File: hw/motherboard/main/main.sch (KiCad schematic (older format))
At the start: 27 parts, among them J1 SWD holes, J2 Conn_ARM_JTAG_SWD_10, J4 STACK_GND, SW1 SW_Push, U1 STM32F303RETx, Y1 HSE

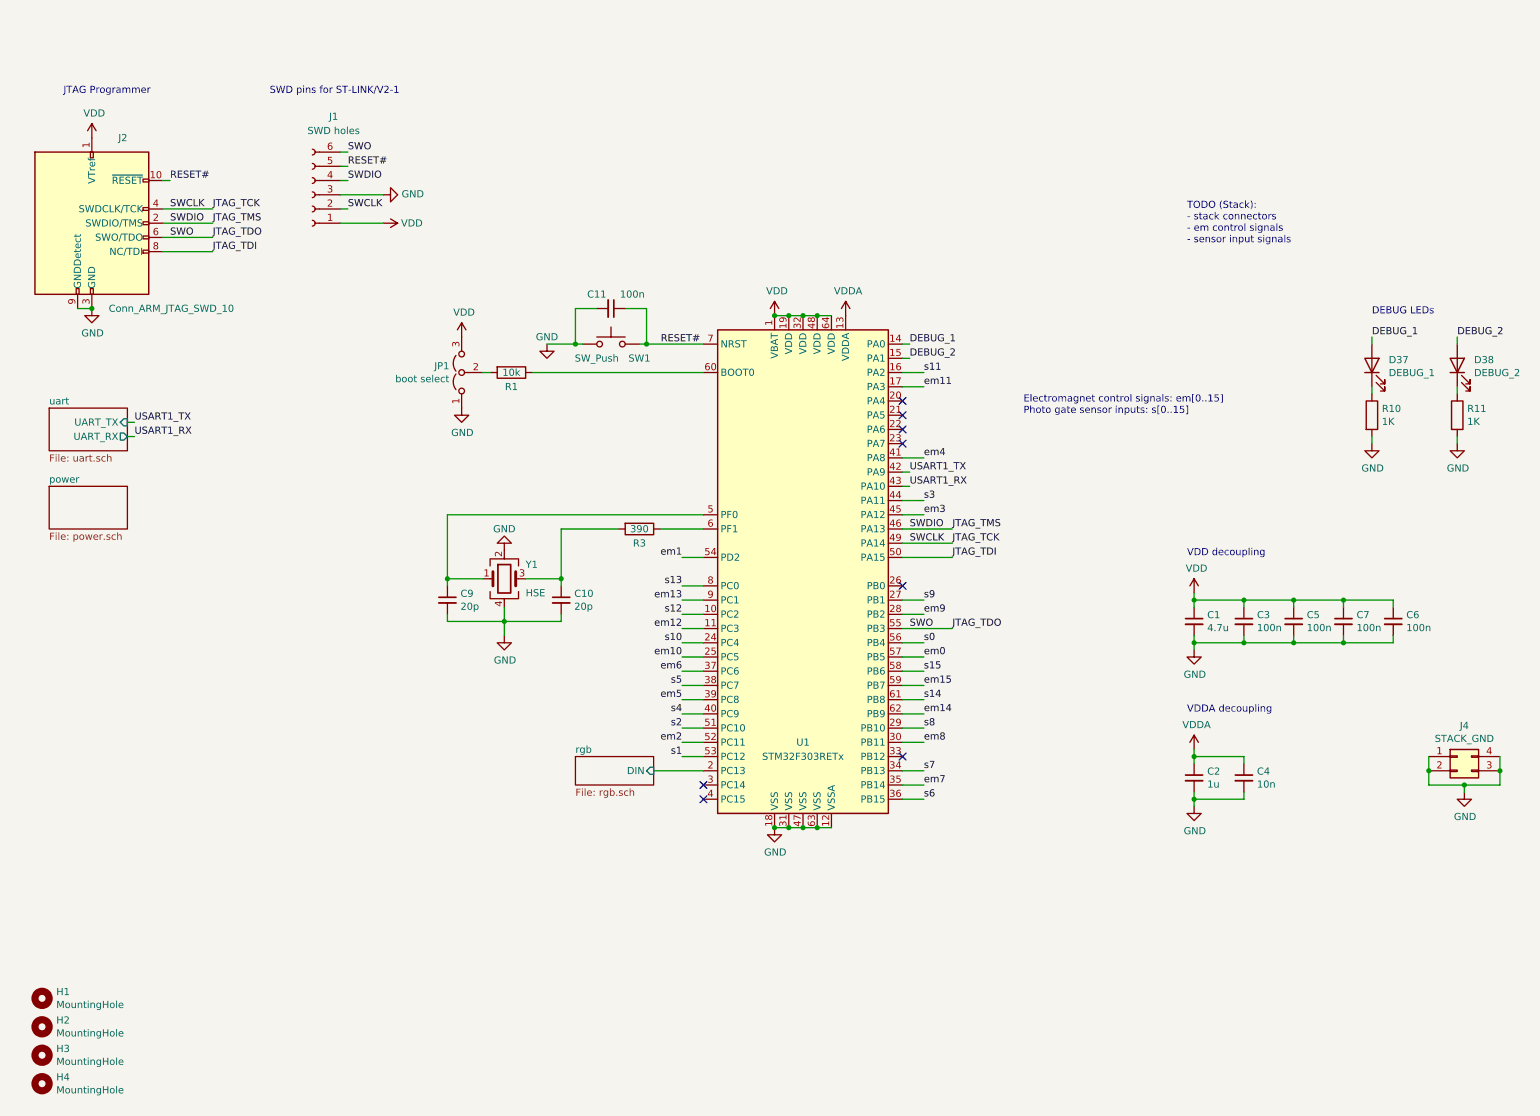
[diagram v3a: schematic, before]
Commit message: Lay out motherboard hardware revision 1
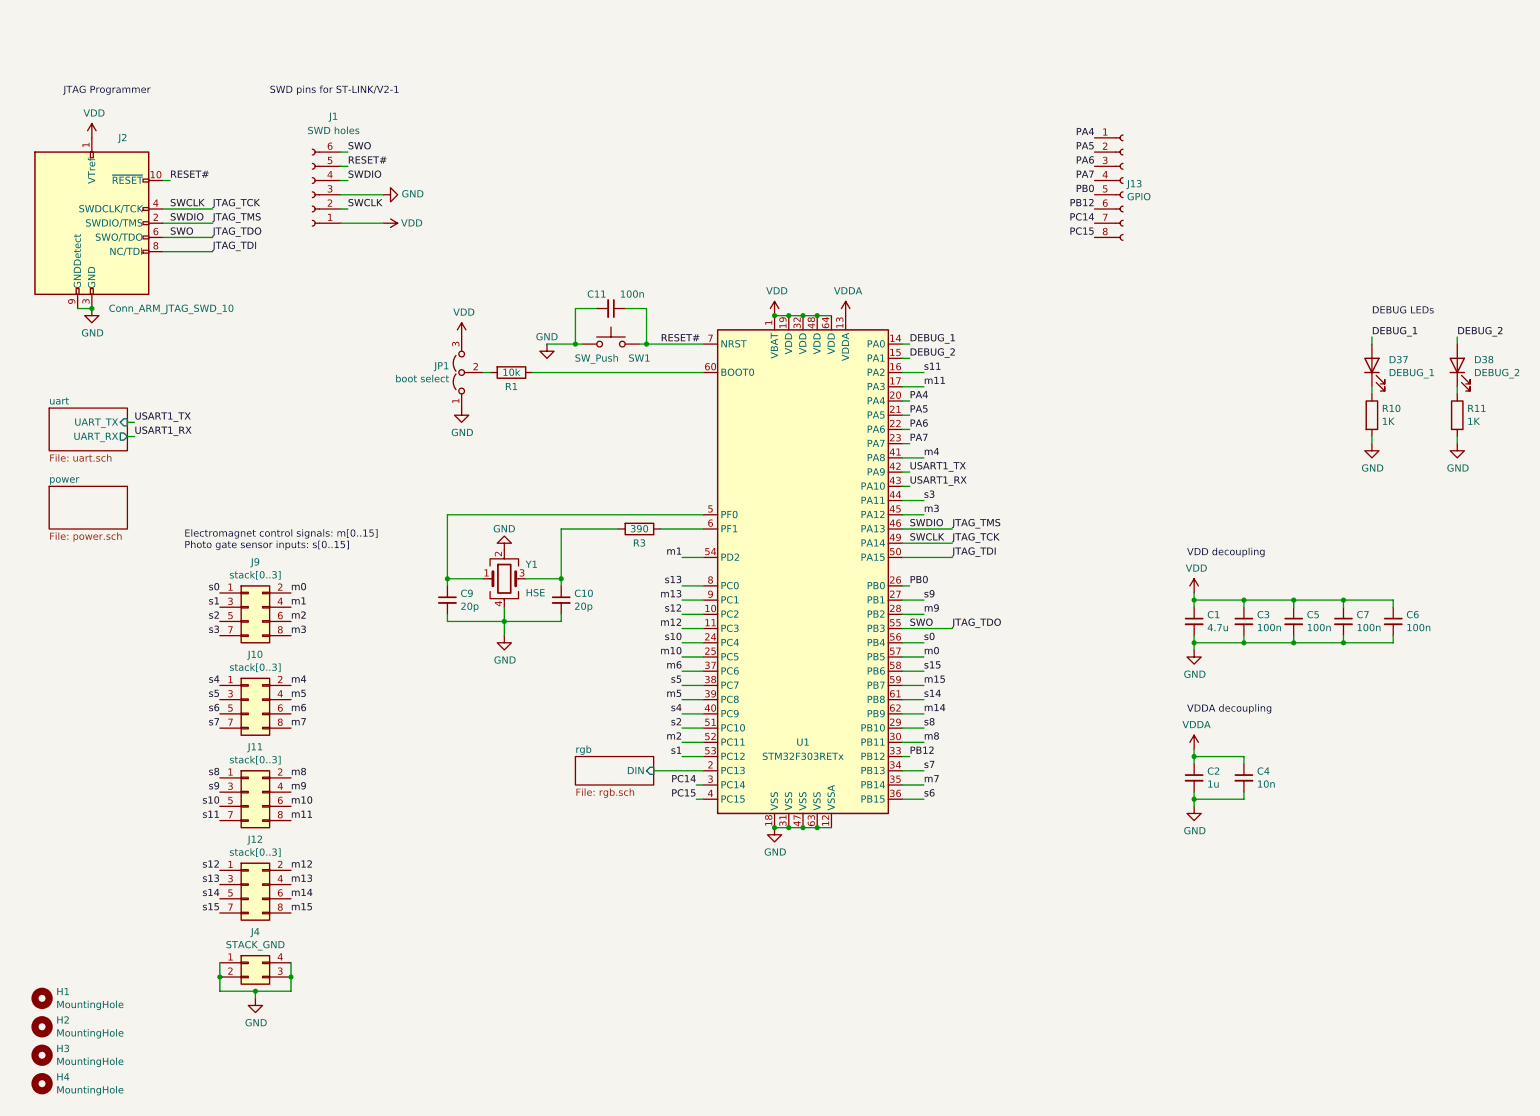
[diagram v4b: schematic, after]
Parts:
- added J10, J11, J12, J9: stack[0..3], Connector_PinSocket_2.54mm:PinSocket_2x04_P2.54mm_Vertical, symbol Connector_Generic:Conn_02x04_Odd_Even
- added J13: GPIO, Connector_PinSocket_2.54mm:PinSocket_1x08_P2.54mm_Vertical, symbol Connector:Conn_01x08_Female
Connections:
- net s0: now also J9.1 (Pin_1)
- net s1: now also J9.3 (Pin_3)
- net s10: now also J11.5 (Pin_5)
- net s11: now also J11.7 (Pin_7)
- net s12: now also J12.1 (Pin_1)
- net s13: now also J12.3 (Pin_3)
- net s14: now also J12.5 (Pin_5)
- net s15: now also J12.7 (Pin_7)
- net s2: now also J9.5 (Pin_5)
- net s3: now also J9.7 (Pin_7)
- net s4: now also J10.1 (Pin_1)
- net s5: now also J10.3 (Pin_3)
- net s6: now also J10.5 (Pin_5)
- net s7: now also J10.7 (Pin_7)
- net s8: now also J11.1 (Pin_1)
- net s9: now also J11.3 (Pin_3)
- net PA4: now reaches U1.20 (PA4)
- net PA4: now also J13.1 (Pin_1)
- net PA5: now reaches U1.21 (PA5)
- net PA5: now also J13.2 (Pin_2)
- net PA6: now reaches U1.22 (PA6)
- net PA6: now also J13.3 (Pin_3)
- net PA7: now reaches U1.23 (PA7)
- net PA7: now also J13.4 (Pin_4)
- net PB0: now reaches U1.26 (PB0)
- net PB0: now also J13.5 (Pin_5)
- net PC14: now reaches U1.3 (PC14)
- net PC14: now also J13.7 (Pin_7)
- net PB12: now reaches U1.33 (PB12)
- net PB12: now also J13.6 (Pin_6)
- net PC15: now reaches U1.4 (PC15)
- net PC15: now also J13.8 (Pin_8)
- net em0 renamed m0
- net m0: now also J9.2 (Pin_2)
- net em1 renamed m1
- net m1: now also J9.4 (Pin_4)
- net em10 renamed m10
- net m10: now also J11.6 (Pin_6)
- net em11 renamed m11
- net m11: now also J11.8 (Pin_8)
- net em12 renamed m12
- net m12: now also J12.2 (Pin_2)
- net em13 renamed m13
- net m13: now also J12.4 (Pin_4)
- net em14 renamed m14
- net m14: now also J12.6 (Pin_6)
- net em15 renamed m15
- net m15: now also J12.8 (Pin_8)
- net em2 renamed m2
- net m2: now also J9.6 (Pin_6)
- net em3 renamed m3
- net m3: now also J9.8 (Pin_8)
- net em4 renamed m4
- net m4: now also J10.2 (Pin_2)
- net em5 renamed m5
- net m5: now also J10.4 (Pin_4)
- net em6 renamed m6
- net m6: now also J10.6 (Pin_6)
- net em7 renamed m7
- net m7: now also J10.8 (Pin_8)
- net em8 renamed m8
- net m8: now also J11.2 (Pin_2)
- net em9 renamed m9
- net m9: now also J11.4 (Pin_4)
- no-connect marks 8 -> 0
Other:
- note added: "Electromagnet control signals: m[0..15]\nPhoto gate sensor inputs: s[0..15]"
- note removed: "Electromagnet control signals: em[0..15]\nPhoto gate sensor inputs: s[0..15]"
- note removed: "TODO (Stack):\n- stack connectors\n- em control signals\n- sensor input signals"
- moved on the sheet: J4

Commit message: Add missing component values.
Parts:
- C1: footprint Capacitor_SMD:C_0603_1608Metric -> Capacitor_SMD:C_0805_2012Metric
- C10, C9: value 20p -> 27p
- R10, R11: value 1K -> 1k
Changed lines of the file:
@@
 F 0 "C1" H 8892 4396 50  0000 L CNN
 F 1 "4.7u" H 8892 4305 50  0000 L CNN
-F 2 "Capacitor_SMD:C_0603_1608Metric" H 8800 4350 50  0001 C CNN
+F 2 "Capacitor_SMD:C_0805_2012Metric" H 8800 4350 50  0001 C CNN
 F 3 "~" H 8800 4350 50  0001 C CNN
 	1    8800 4350
@@
 P 3550 4200
 F 0 "C9" H 3642 4246 50  0000 L CNN
-F 1 "20p" H 3642 4155 50  0000 L CNN
+F 1 "27p" H 3642 4155 50  0000 L CNN
 F 2 "Capacitor_SMD:C_0603_1608Metric" H 3550 4200 50  0001 C CNN
 F 3 "~" H 3550 4200 50  0001 C CNN
@@
 P 4350 4200
 F 0 "C10" H 4442 4246 50  0000 L CNN
-F 1 "20p" H 4442 4155 50  0000 L CNN
+F 1 "27p" H 4442 4155 50  0000 L CNN
 F 2 "Capacitor_SMD:C_0603_1608Metric" H 4350 4200 50  0001 C CNN
 F 3 "~" H 4350 4200 50  0001 C CNN
@@
 P 10650 2900
 F 0 "R11" H 10720 2946 50  0000 L CNN
-F 1 "1K" H 10720 2855 50  0000 L CNN
+F 1 "1k" H 10720 2855 50  0000 L CNN
 F 2 "Resistor_SMD:R_0805_2012Metric" V 10580 2900 50  0001 C CNN
 F 3 "~" H 10650 2900 50  0001 C CNN
@@
 P 10050 2900
 F 0 "R10" H 10120 2946 50  0000 L CNN
-F 1 "1K" H 10120 2855 50  0000 L CNN
+F 1 "1k" H 10120 2855 50  0000 L CNN
 F 2 "Resistor_SMD:R_0805_2012Metric" V 9980 2900 50  0001 C CNN
 F 3 "~" H 10050 2900 50  0001 C CNN

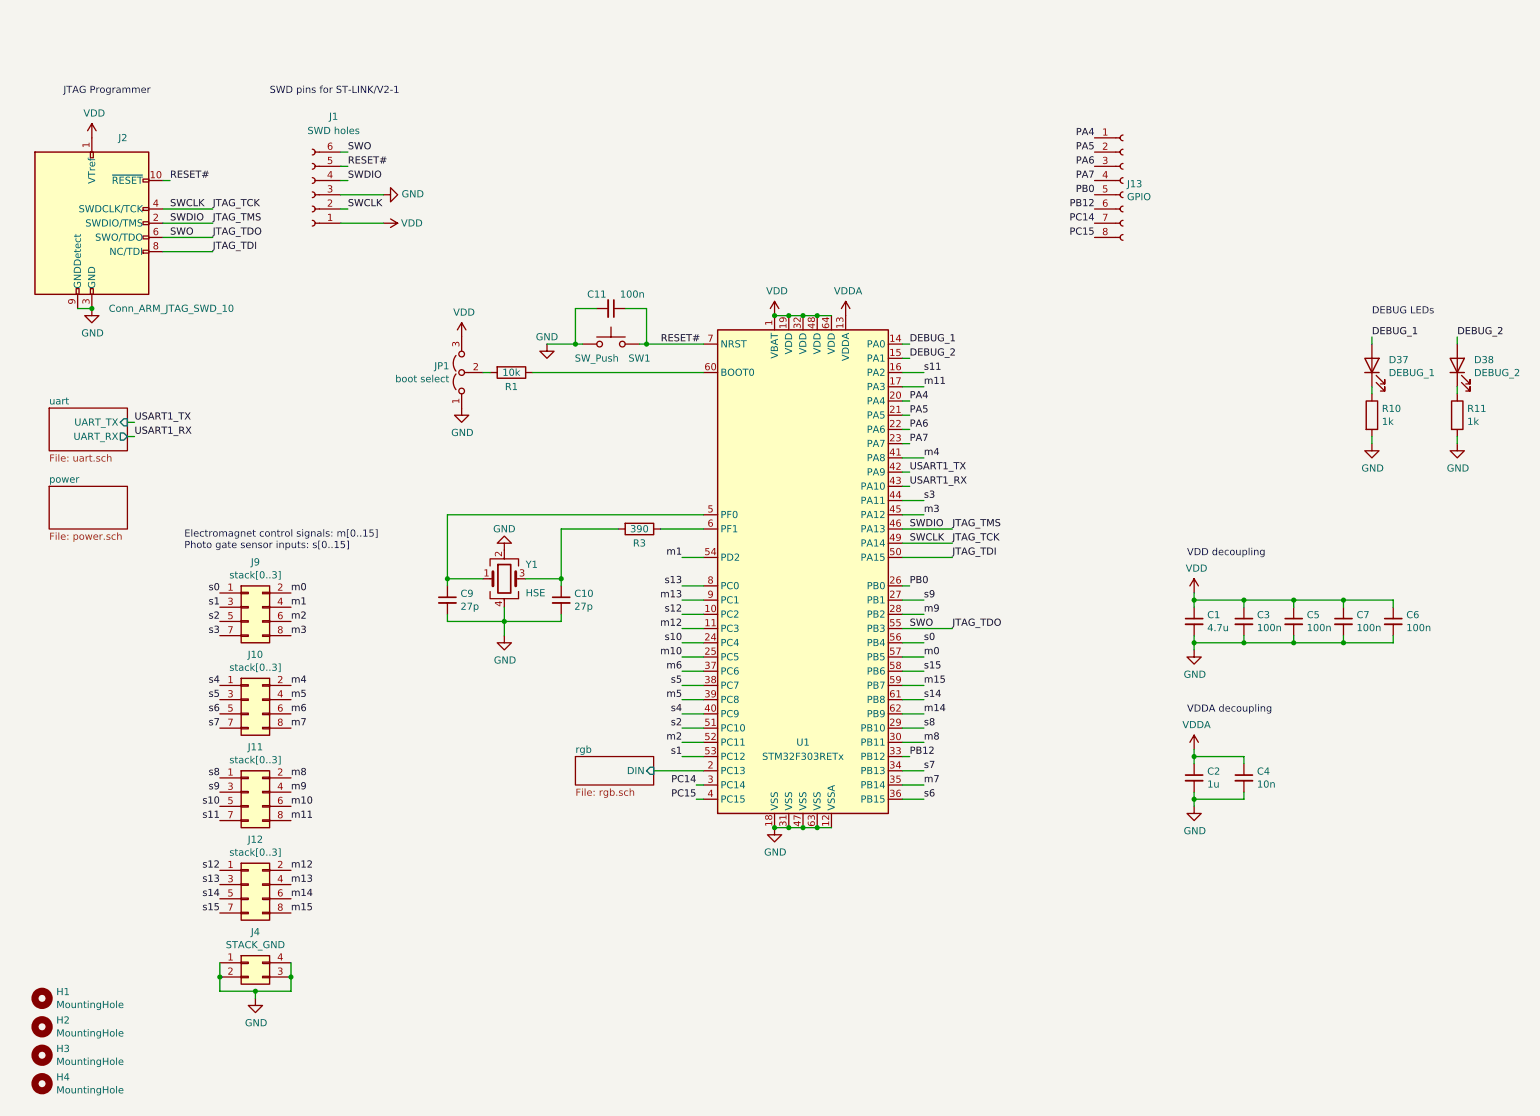
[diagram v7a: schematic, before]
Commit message: wip: fix motherboard v1.1 bugs
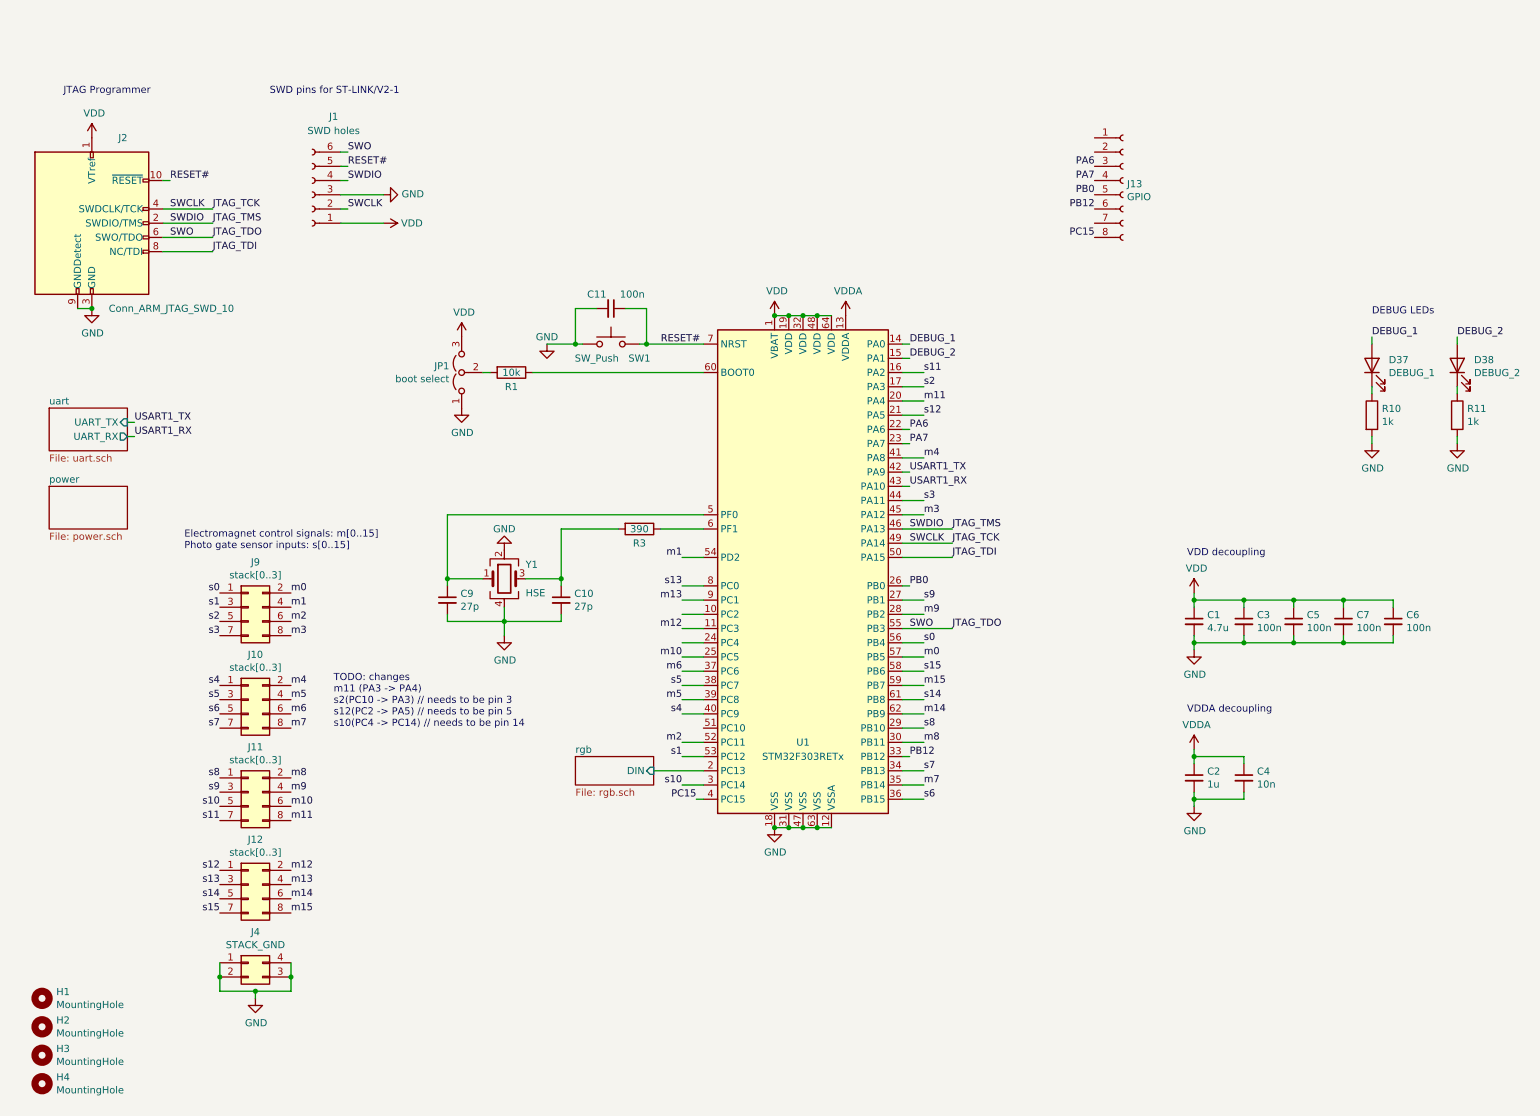
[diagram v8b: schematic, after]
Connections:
- net m11: now also U1.20 (PA4); no longer U1.17 (PA3)
- net s10: now also U1.3 (PC14); no longer U1.24 (PC4)
- net s12: now also U1.21 (PA5); no longer U1.10 (PC2)
- net s2: now also U1.17 (PA3); no longer U1.51 (PC10)
- net PA4: no longer names the net of J13.1 (Pin_1)
- net PA4: no longer U1.20 (PA4)
- net PA5: no longer names the net of J13.2 (Pin_2)
- net PA5: no longer U1.21 (PA5)
- net PC14: no longer names the net of J13.7 (Pin_7)
- net PC14: no longer U1.3 (PC14)
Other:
- note added: "TODO: changes\nm11 (PA3 -> PA4)\ns2(PC10 -> PA3) // needs to be pin 3\ns12(PC2 -> PA5) // needs to be pin 5\ns10(PC4 -> PC14) // needs to be pin 14\n"
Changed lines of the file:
@@
 Wire Wire Line
 	5200 5200 5350 5200
-Text Label 5200 5100 2    50   ~ 0
+Text Label 6900 2700 0    50   ~ 0
 s2
-Wire Wire Line
-	5350 5100 5200 5100
 Text Label 6900 3600 0    50   ~ 0
 m3
@@
 Wire Wire Line
 	5200 4600 5350 4600
-Text Label 5200 4500 2    50   ~ 0
+Text Label 5200 5500 2    50   ~ 0
 s10
 Wire Wire Line
 	5200 4500 5350 4500
-Text Label 6900 2700 0    50   ~ 0
+Text Label 6900 2800 0    50   ~ 0
 m11
 Wire Wire Line
@@
 Wire Wire Line
 	5200 4400 5350 4400
-Text Label 5200 4300 2    50   ~ 0
+Text Label 6900 2900 0    50   ~ 0
 s12
 Wire Wire Line
@@
 	1    0    0    -1
 $EndComp
-Text Label 6800 2800 0    50   ~ 0
-PA4
-Text Label 6800 2900 0    50   ~ 0
-PA5
 Text Label 6800 3000 0    50   ~ 0
 PA6
@@
 	6800 3000 6750 3000
 Wire Wire Line
-	6800 2900 6750 2900
-Wire Wire Line
-	6800 2800 6750 2800
-Text Label 8100 950  2    50   ~ 0
-PA4
-Text Label 8100 1050 2    50   ~ 0
-PA5
+	6900 2900 6750 2900
+Wire Wire Line
+	6900 2800 6750 2800
 Text Label 8100 1150 2    50   ~ 0
 PA6
@@
 Text Label 8100 1450 2    50   ~ 0
 PB12
-Text Label 5300 5500 2    50   ~ 0
-PC14
 Text Label 5300 5600 2    50   ~ 0
 PC15
 Wire Wire Line
-	5300 5500 5350 5500
+	5200 5500 5350 5500
 Wire Wire Line
 	5300 5600 5350 5600
-Text Label 8100 1550 2    50   ~ 0
-PC14
 Text Label 8100 1650 2    50   ~ 0
 PC15
@@
 	1    0    0    -1
 $EndComp
+Text Notes 2750 5100 0    50   ~ 0
+TODO: changes\nm11 (PA3 -> PA4)\ns2(PC10 -> PA3) // needs to be pin 3\ns12(PC2 -> PA5) // needs to be pin 5\ns10(PC4 -> PC14) // needs to be pin 14\n
 $EndSCHEMATC
